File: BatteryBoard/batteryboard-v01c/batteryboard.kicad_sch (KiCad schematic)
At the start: 30 parts, among them J1 KEYSTONE-1042, J2 KEYSTONE-1042, J3 KEYSTONE-1042, J4 KEYSTONE-1042, J5 KEYSTONE-1042, J6 KEYSTONE-1042, J7 MOLEX 5023520601, J8 Screw_Terminal_01x02, Q1 IRF7458, Q2 IRF7458, Q3 IRLML2803, U1 R5460N233AF

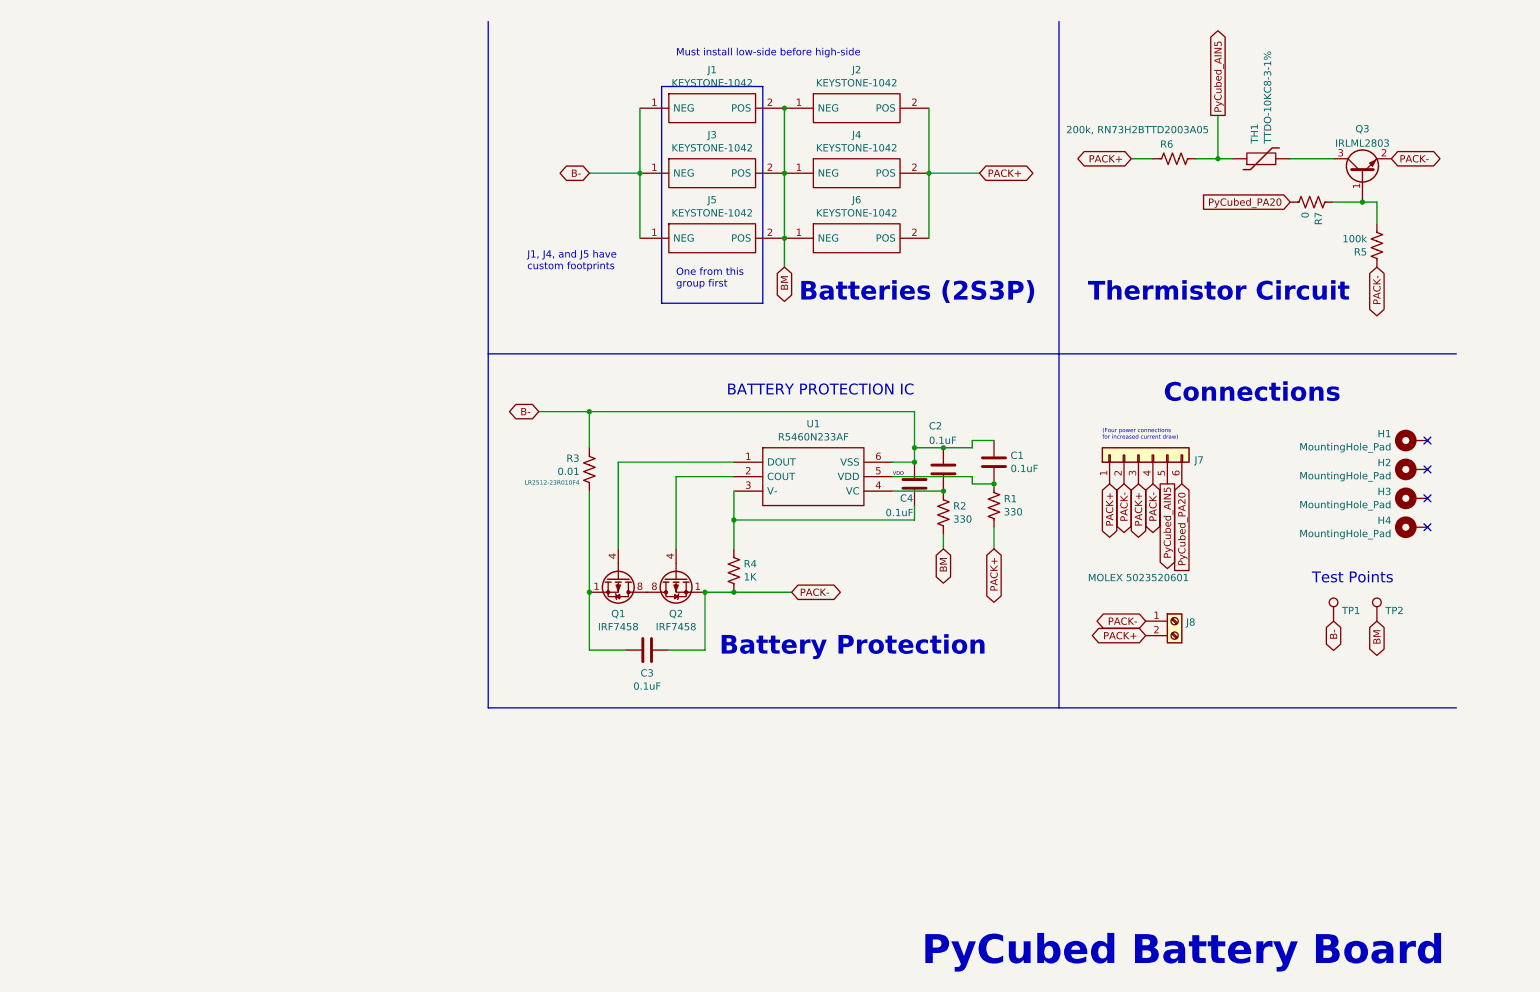
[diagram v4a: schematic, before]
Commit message: Updated main board with heater circuit
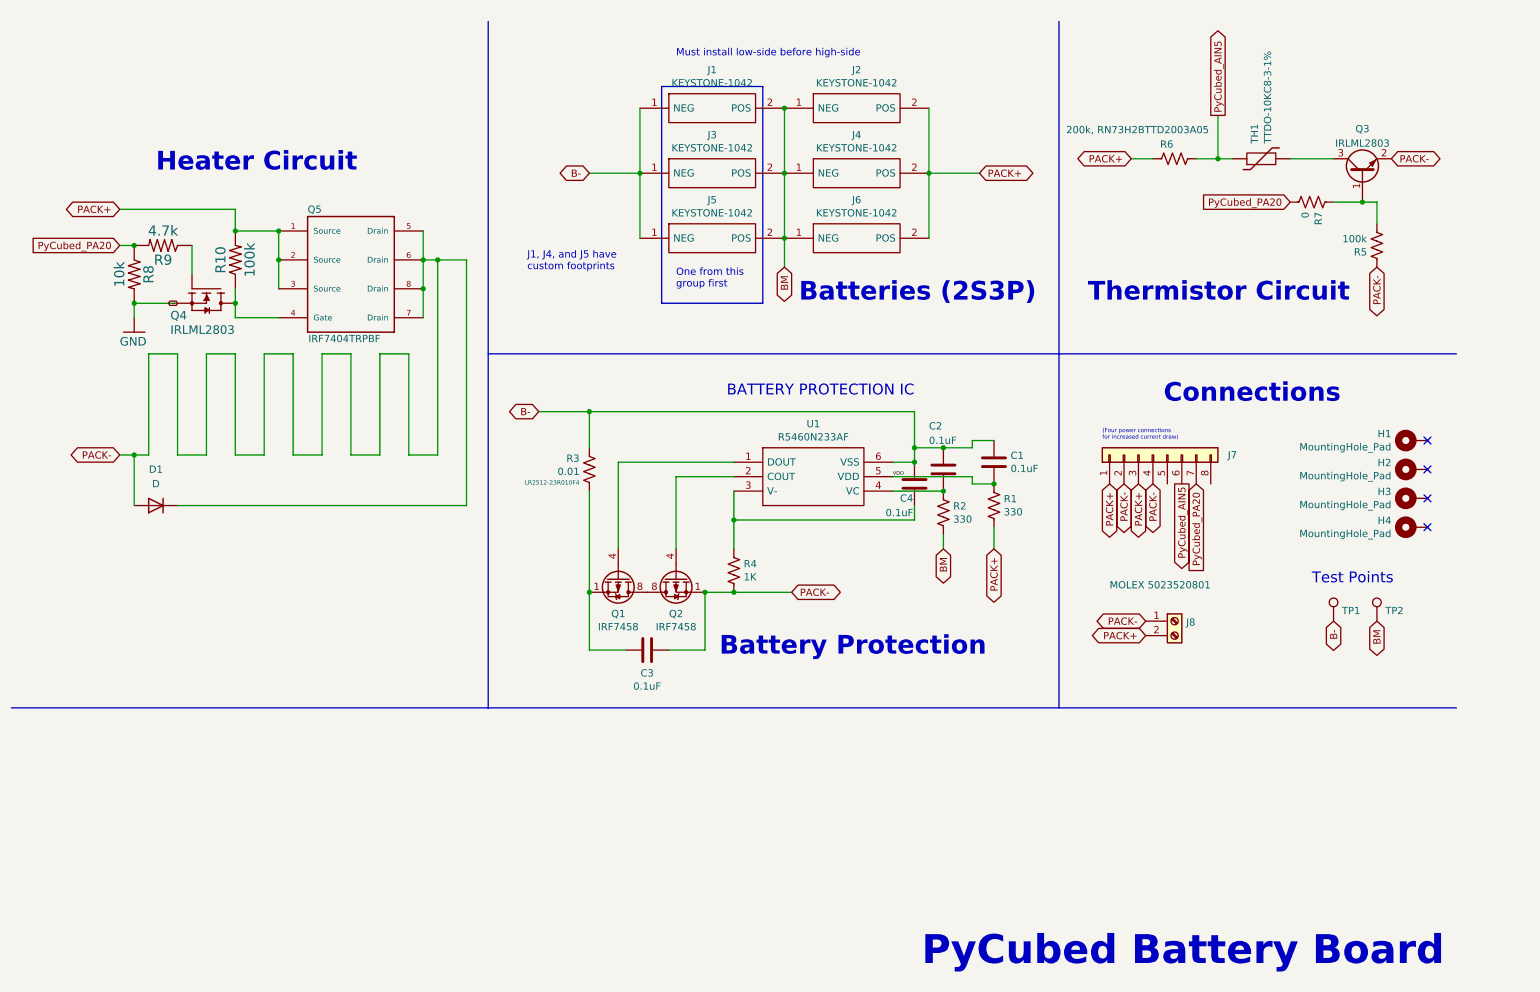
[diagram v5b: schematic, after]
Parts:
- removed J7: MOLEX 5023520601, batteryboard:5023520600, symbol Connector_Generic:Conn_01x06
- added D1: D, Diode_SMD:D_SOD-123F, symbol Device:D
- added J7: MOLEX 5023520801, batteryboard_local:CONN_502352-0801_MOL, symbol Connector_Generic:Conn_01x08
- added Q4: IRLML2803, batteryboard_local:SOT-23, symbol mainboard:IRLML2803TRPBF
- added Q5: IRF7404TRPBF, batteryboard_local:IRF7404TRPBF, symbol mainboard:IRF7404TRPBF
- added R10: 100k, Resistor_SMD:R_0603_1608Metric, symbol mainboard:RESISTOR0603
- added R8: 10k, Resistor_SMD:R_0603_1608Metric, symbol mainboard:RESISTOR0603
- added R9: 4.7k, Resistor_SMD:R_0603_1608Metric, symbol mainboard:RESISTOR0603
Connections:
- net PACK+: now also J7.1 (Pin_1), J7.3 (Pin_3), Q5.1 (Source), Q5.2 (Source), Q5.3 (Source), R10.2
- net PACK-: now also D1.1 (K), D1.2 (A), J7.2 (Pin_2), J7.4 (Pin_4), Q5.5 (Drain), Q5.6 (Drain), Q5.7 (Drain), Q5.8 (Drain)
- net PyCubed_AIN5: now also J7.6 (Pin_6)
- net PyCubed_PA20: now also J7.7 (Pin_7), R8.1, R9.2
- new net: Q4.1 (G), R9.1
- new net: Q4.3 (D), Q5.4 (Gate), R10.1
- new net GND: Q4.2 (S), R8.2
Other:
- note added: "Heater Circuit"

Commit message: Updated PCB
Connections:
- net PyCubed_PA20: no longer R8.1, R9.2
- net PyCubed_HIN: now reaches J7.5 (Pin_5)
- net PyCubed_HIN: now also R8.1, R9.2
- net VBATT_SENSE: now reaches J7.8 (Pin_8)
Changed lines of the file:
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@@
   (global_label "PyCubed_AIN5" (shape output) (at 218.44 95.25 270) (fields_autoplaced)
     (effects (font (size 1.27 1.27)) (justify right))
-    (property "Intersheetrefs" "${INTERSHEET_REFS}" (at 218.44 110.7458 90)
+    (property "Intersheetrefs" "${INTERSHEET_REFS}" (at 218.44 110.8252 90)
+      (effects (font (size 1.27 1.27)) (justify right) hide)
+    )
+  )
+  (global_label "PyCubed_HIN" (shape input) (at 215.9 95.25 270) (fields_autoplaced)
+    (effects (font (size 1.27 1.27)) (justify right))
+    (property "Intersheetrefs" "${INTERSHEET_REFS}" (at 215.9 109.8576 90)
       (effects (font (size 1.27 1.27)) (justify right) hide)
     )
@@
     (effects (font (size 1.27 1.27)) (justify right))
     (property "Intersheetrefs" "${INTERSHEET_REFS}" (at 221.45 45.72 0)
-      (effects (font (size 1.27 1.27)) (justify right) hide)
-    )
-  )
-  (global_label "PyCubed_PA20" (shape input) (at 31.75 53.34 180) (fields_autoplaced)
-    (effects (font (size 1.27 1.27)) (justify right))
-    (property "Intersheetrefs" "${INTERSHEET_REFS}" (at 15.6306 53.34 0)
       (effects (font (size 1.27 1.27)) (justify right) hide)
     )
@@
     )
   )
+  (global_label "PyCubed_HIN" (shape input) (at 31.75 53.34 180) (fields_autoplaced)
+    (effects (font (size 1.27 1.27)) (justify right))
+    (property "Intersheetrefs" "${INTERSHEET_REFS}" (at 17.1424 53.34 0)
+      (effects (font (size 1.27 1.27)) (justify right) hide)
+    )
+  )
   (global_label "PACK+" (shape bidirectional) (at 205.74 95.25 270) (fields_autoplaced)
     (effects (font (size 1.27 1.27)) (justify right))
@@
       (effects (font (size 1.27 1.27)) (justify right) hide)
     )
+  )
+  (global_label "VBATT_SENSE" (shape output) (at 223.52 95.25 270) (fields_autoplaced)
+    (effects (font (size 1.27 1.27)) (justify right))
+    (property "Intersheetrefs" "${INTERSHEET_REFS}" (at 223.52 109.9785 90)
+      (effects (font (size 1.27 1.27)) (justify right) hide)
+    )

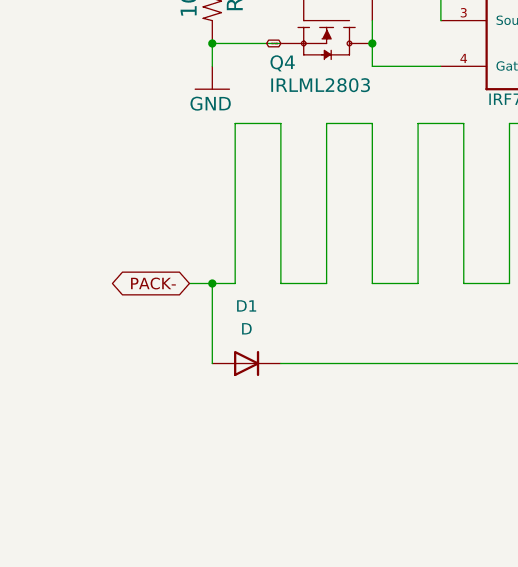
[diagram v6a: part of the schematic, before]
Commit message: Added pycubed heater input and output to battery sense
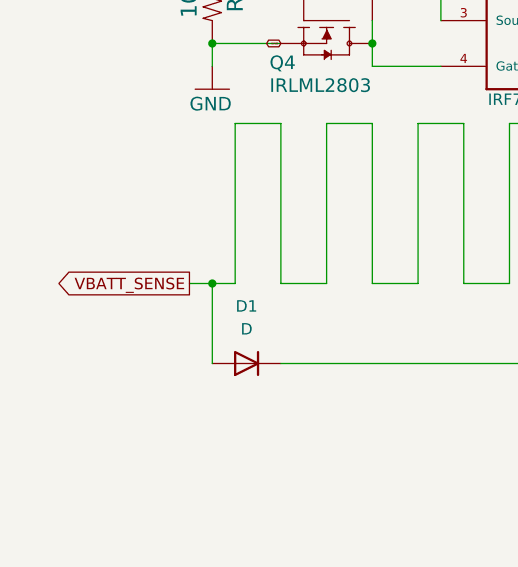
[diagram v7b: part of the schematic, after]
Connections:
- net PACK-: no longer D1.1 (K), D1.2 (A), Q5.5 (Drain), Q5.6 (Drain), Q5.7 (Drain), Q5.8 (Drain)
- net VBATT_SENSE: now also D1.1 (K), D1.2 (A), Q5.5 (Drain), Q5.6 (Drain), Q5.7 (Drain), Q5.8 (Drain)
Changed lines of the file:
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@@
-    )
-  )
-  (global_label "PACK-" (shape bidirectional) (at 31.75 90.17 180) (fields_autoplaced)
-    (effects (font (size 1.27 1.27)) (justify right))
-    (property "Intersheetrefs" "${INTERSHEET_REFS}" (at 21.9955 90.17 0)
-      (effects (font (size 1.27 1.27)) (justify right) hide)
     )
   )
@@
       (effects (font (size 1.27 1.27)) (justify right) hide)
     )
+  )
+  (global_label "VBATT_SENSE" (shape output) (at 31.75 90.17 180) (fields_autoplaced)
+    (effects (font (size 1.27 1.27)) (justify right))
+    (property "Intersheetrefs" "${INTERSHEET_REFS}" (at 17.0215 90.17 0)
+      (effects (font (size 1.27 1.27)) (justify right) hide)
+    )
